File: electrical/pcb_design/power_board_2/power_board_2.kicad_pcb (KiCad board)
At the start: 4 copper layers, 82.5 x 82.5 mm, 92 parts, among them J1 STLINK, J2 Molex_504050-1291, J3 Molex_504050-1291, J4 Power Interconnect, Q1 CSD16342Q5A, Q2 CSD16342Q5A, Q3 CSD16342Q5A, U1 STM32L452RCTx, U2 TCAN330DR, U3 PAC1934T-I/JQ, U8 TPS63900

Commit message: finish initial component selection and start layout
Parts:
- removed BT1, BT2, BT3: Battery_Cell, footprints:BAT_1043
- removed JP13, JP2, JP4: SolderJumper_2_Open, Jumper:SolderJumper-2_P1.3mm_Open_RoundedPad1.0x1.5mm
- removed JP14: 0x10, Jumper:SolderJumper-2_P1.3mm_Open_RoundedPad1.0x1.5mm
- removed JP15: 0xEF, Jumper:SolderJumper-2_P1.3mm_Open_RoundedPad1.0x1.5mm
- removed Q1, Q2, Q3: CSD16342Q5A, Package_SON:VSON-8_3.3x3.3mm_P0.65mm_NexFET
- removed R10: 10m, Resistor_SMD:R_2512_6332Metric
- removed R13: 9k31, footprints:Nondescript_R_0402_1005Metric
- removed R51: 36k5, footprints:Nondescript_R_0603_1608Metric
- removed TH1: 10k NTC, footprints:Nondescript_R_0402_1005Metric
- removed TP7: TEMP, footprints:TestPoint_Pad_D1.5mm
- removed TP8: VBATT, footprints:TestPoint_Pad_D1.5mm
- added C18: 1u, footprints:Nondescript_C_0402_1005Metric, F.Cu at (159.8, 94.5)
- added C19: 4.7u, footprints:Nondescript_C_0402_1005Metric, F.Cu at (159.8, 96.5)
- added C20: 22n, footprints:Nondescript_C_0402_1005Metric, F.Cu at (173.3, 115.9)
- added C21: 22n, footprints:Nondescript_C_0402_1005Metric, F.Cu at (173.3, 117.9)
- added C22: 47u, footprints:Nondescript_C_0402_1005Metric, F.Cu at (173.3, 119.8)
- added C23: 1u, footprints:Nondescript_C_0402_1005Metric, F.Cu at (173.3, 121.8)
- added C24: 4.7u, footprints:Nondescript_C_0402_1005Metric, F.Cu at (173.3, 123.8)
- added C25: 10p, footprints:Nondescript_C_0402_1005Metric, F.Cu at (173.3, 125.7)
- added C26: 22n, footprints:Nondescript_C_0402_1005Metric, F.Cu at (173.3, 82.4)
- added C28: 47u, footprints:Nondescript_C_0402_1005Metric, F.Cu at (173.3, 86.4)
- added C29: 1u, footprints:Nondescript_C_0402_1005Metric, F.Cu at (173.3, 88.4)
- added C30: 4.7u, footprints:Nondescript_C_0402_1005Metric, F.Cu at (173.3, 90.3)
- added C31: 10p, footprints:Nondescript_C_0402_1005Metric, F.Cu at (173.3, 92.3)
- added C32: 22n, footprints:Nondescript_C_0402_1005Metric, F.Cu at (173.3, 99.2)
- added C33: 22n, footprints:Nondescript_C_0402_1005Metric, F.Cu at (173.3, 101.1)
- added C34: 47u, footprints:Nondescript_C_0402_1005Metric, F.Cu at (173.3, 103.1)
- added C35: 1u, footprints:Nondescript_C_0402_1005Metric, F.Cu at (173.3, 105.1)
- added C36: 4.7u, footprints:Nondescript_C_0402_1005Metric, F.Cu at (173.3, 107.0)
- added C37: 10p, footprints:Nondescript_C_0402_1005Metric, F.Cu at (173.3, 109.0)
- added D10: SM74611KTTR, footprints:SM74611, F.Cu at (101.6, 112.4)
- added D2: SM74611KTTR, footprints:SM74611, F.Cu at (65.3, 87.7)
- added D3: SM74611KTTR, footprints:SM74611, F.Cu at (65.3, 100.0)
- added D4: SM74611KTTR, footprints:SM74611, F.Cu at (65.3, 112.4)
- added D5: SM74611KTTR, footprints:SM74611, F.Cu at (83.4, 87.7)
- added D6: SM74611KTTR, footprints:SM74611, F.Cu at (83.4, 100.0)
- added D7: SM74611KTTR, footprints:SM74611, F.Cu at (83.4, 112.4)
- added D8: SM74611KTTR, footprints:SM74611, F.Cu at (101.6, 87.7)
- added D9: SM74611KTTR, footprints:SM74611, F.Cu at (101.6, 100.0)
- added J5: Molex_504050-0691, footprints:Molex_504050-0691, F.Cu at (68.6, 126.6)
- added J6: Molex_504050-0691, footprints:Molex_504050-0691, F.Cu at (68.6, 136.7)
- added JP7: SolderJumper_2_Open, Jumper:SolderJumper-2_P1.3mm_Open_RoundedPad1.0x1.5mm, F.Cu at (151.6, 112.8)
- added JP8: SolderJumper_2_Open, Jumper:SolderJumper-2_P1.3mm_Open_RoundedPad1.0x1.5mm, F.Cu at (151.6, 116.3)
- added JP9: SolderJumper_2_Open, Jumper:SolderJumper-2_P1.3mm_Open_RoundedPad1.0x1.5mm, F.Cu at (151.6, 119.9)
- added L2: 6.8u, footprints:LQH44PN_PR_MUR, F.Cu at (181.6, 124.6)
- added L3: 6.8u, footprints:LQH44PN_PR_MUR, F.Cu at (181.6, 91.1)
- added L4: 6.8u, footprints:LQH44PN_PR_MUR, F.Cu at (181.6, 107.9)
- added R11: 9k31, footprints:Nondescript_R_0402_1005Metric, F.Cu at (140.1, 111.8)
- added R12: 9k31, footprints:Nondescript_R_0402_1005Metric, F.Cu at (140.1, 113.8)
- added R15: 33, footprints:Nondescript_R_0402_1005Metric, F.Cu at (143.0, 105.9)
- added R16: 33, footprints:Nondescript_R_0402_1005Metric, F.Cu at (143.0, 107.8)
- added R18: 12k4, footprints:Nondescript_R_0402_1005Metric, F.Cu at (200.3, 99.0)
- added R19: 12k4, footprints:Nondescript_R_0402_1005Metric, F.Cu at (200.3, 101.0)
- added R42: 1M, footprints:Nondescript_R_0402_1005Metric, F.Cu at (176.2, 111.9)
- added R43: 1, Resistor_SMD:R_2512_6332Metric, F.Cu at (115.0, 93.7)
- added R44: 1, Resistor_SMD:R_2512_6332Metric, F.Cu at (115.0, 98.6)
- added R45: 1, Resistor_SMD:R_2512_6332Metric, F.Cu at (115.0, 103.5)
- added R46: 1, Resistor_SMD:R_2512_6332Metric, F.Cu at (115.0, 108.4)
- added U10: LTC3130EUDC-PBF, footprints:LTC3130, F.Cu at (186.3, 101.5)
- added U11: AD5242BRUZ1M, footprints:AD5242, F.Cu at (179.1, 101.6)
- added U12: PAC1932T-I/JQ, footprints:PAC1934, F.Cu at (77.1, 121.8)
- added U13: PAC1932T-I/JQ, footprints:PAC1934, F.Cu at (77.1, 128.0)
- added U4: BQ24075RGTR, footprints:BQ2407x, F.Cu at (163.9, 94.3)
- added U5: MCP4661-103E/ST, footprints:MCP4661, F.Cu at (153.8, 94.9)
- added U6: LTC3130EUDC-PBF, footprints:LTC3130, F.Cu at (186.3, 118.2)
- added U7: AD5242BRUZ1M, footprints:AD5242, F.Cu at (179.1, 118.3)
- added U9: AD5242BRUZ1M, footprints:AD5242, F.Cu at (179.1, 84.8)
- C1, C14, C6, C9: value 100n -> 1u; moved to F.Cu
- C10, C15, C16: value 1u -> 100n; moved to F.Cu
- C11: value 1u -> 22u; moved to F.Cu
- C12: value 1u -> 10u; moved to F.Cu
- C13: value 100n -> 22u; moved to F.Cu
- C17: value 100n -> 4.7u; moved to F.Cu
- C2, C3, C7, C8, D1, J2, J3, JP1, JP10, JP3, JP5, JP6, L1, R1, R3, R4, R6, R9, TP4, U1: moved to F.Cu
- C27: value 22u -> 22n; footprint footprints:Nondescript_C_0603_1608Metric -> footprints:Nondescript_C_0402_1005Metric; moved to F.Cu
- C4: value 10u -> 1u; footprint footprints:Nondescript_C_0603_1608Metric -> footprints:Nondescript_C_0402_1005Metric; moved to F.Cu
- C5: value 22u -> 100n; footprint footprints:Nondescript_C_0603_1608Metric -> footprints:Nondescript_C_0402_1005Metric; moved to F.Cu
- J4: value Power Interconnect -> Molex_504050-0691; moved to F.Cu
- PCB1: footprint footprints:Battery_Board_Shape_Space_Invader_2 -> footprints:Core_Board_Shape_Space_Invader_2
- R14, R25, R26: value 9k31 -> 33; moved to F.Cu
- R17: value 23k2 -> 33; moved to F.Cu
- R2, R5, R7, R8: value 33 -> 9k31; moved to F.Cu
- R20, R21: value 1k58 -> 1; footprint footprints:Nondescript_R_0402_1005Metric -> Resistor_SMD:R_2512_6332Metric; moved to F.Cu
- R22: value 23k2 -> 10m; footprint footprints:Nondescript_R_0402_1005Metric -> Resistor_SMD:R_2512_6332Metric; moved to F.Cu
- R23: value 9k31 -> 36k5; footprint footprints:Nondescript_R_0402_1005Metric -> footprints:Nondescript_R_0603_1608Metric; moved to F.Cu
- R24: value 10m -> 33; footprint Resistor_SMD:R_2512_6332Metric -> footprints:Nondescript_R_0402_1005Metric; moved to F.Cu
- R27: value 10m -> 60; footprint Resistor_SMD:R_2512_6332Metric -> footprints:Nondescript_R_0402_1005Metric; moved to F.Cu
- R28: value 9k31 -> 60; moved to F.Cu
- R29: value 10m -> 10k; footprint Resistor_SMD:R_2512_6332Metric -> footprints:Nondescript_R_0402_1005Metric; moved to F.Cu
- R30: value 9k31 -> 10m; footprint footprints:Nondescript_R_0402_1005Metric -> Resistor_SMD:R_2512_6332Metric; moved to F.Cu
- R31, R35: value 0 -> 4M; footprint Resistor_SMD:R_2512_6332Metric -> footprints:Nondescript_R_0402_1005Metric; moved to F.Cu
- R32, R36, R40: value 0 -> 200k; footprint Resistor_SMD:R_2512_6332Metric -> footprints:Nondescript_R_0402_1005Metric; moved to F.Cu
- R33, R41: value 0 -> 100k; footprint Resistor_SMD:R_2512_6332Metric -> footprints:Nondescript_R_0402_1005Metric; moved to F.Cu
- R34: value 0 -> 1M; footprint Resistor_SMD:R_2512_6332Metric -> footprints:Nondescript_R_0402_1005Metric; moved to F.Cu
- R37: value 33 -> 100k; moved to F.Cu
- R38: value 33 -> 1M; moved to F.Cu
- R39: value 33 -> 4M; moved to F.Cu
- R49, R50: value 60 -> 9k31; moved to F.Cu
- TP1: value VBUS -> BOARD_ID_POWER
- TP2: value BOARD_ID_POWER -> BOARD_ID_SENSE; moved to F.Cu
- TP3: value GND -> VBUS
- TP5: value BOARD_ID_SENSE -> +3V3; moved to F.Cu
- TP6: value +3V3 -> GND
- U2: value TCAN330DR -> TPS63900; footprint footprints:SOIC127P600X175-8N -> Package_SON:WSON-10-1EP_2.5x2.5mm_P0.5mm_EP1.2x2mm_ThermalVias; moved to F.Cu
- U3: value PAC1934T-I/JQ -> TCAN330DR; footprint footprints:UQFN-16-1EP_4x4mm_P0.65mm_EP2.6x2.6mm -> footprints:SOIC127P600X175-8N; moved to F.Cu
- U8: value TPS63900 -> LTC3130EUDC-PBF; footprint Package_SON:WSON-10-1EP_2.5x2.5mm_P0.5mm_EP1.2x2mm -> footprints:LTC3130; moved to F.Cu
- moved PCB1 103.9 mm to (33.9, 80.8)
- moved R49 81.9 mm to (75.4, 132.1), turned to 0 degrees
- moved R50 79.6 mm to (75.4, 134.1), turned to 0 degrees
- moved J1 79.2 mm to (197.9, 109.6), turned to 0 degrees
- moved TP6 76.4 mm to (192.7, 93.9)
- moved R24 70.6 mm to (192.4, 108.1), turned to 0 degrees
- moved R37 61.6 mm to (176.2, 93.2), turned to 0 degrees
- moved TP2 57.1 mm to (192.7, 103.3), turned to 0 degrees
- moved R22 55.7 mm to (198.9, 89.8), turned to 0 degrees
- moved J2 55.3 mm to (134.4, 86.1), turned to 0 degrees
- moved R39 55.1 mm to (176.2, 105.9), turned to 0 degrees
- moved TP5 54.9 mm to (192.7, 90.3), turned to 0 degrees
- moved R38 54.6 mm to (176.2, 95.2), turned to 0 degrees
- moved U2 54.5 mm to (200.2, 83.8), turned to 0 degrees
- moved R35 53.5 mm to (176.2, 89.2)
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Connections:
- C1 pad 1: /NRST -> +3V3
- C10 pad 1: +3V3 -> /BOOT0
- C11 pad 1: +3V3 -> VBUS
- C12 pad 1: +3V3 -> VBUS
- C13 pad 1: +3V3 -> /Charger/BOARD_load+
- C16 pad 1: +3V3 -> GND
- C16 pad 2: GND -> Net-(C16-Pad2)
- C17 pad 1: +3V3 -> Net-(C17-Pad1)
- C2 pad 1: /BOOT0 -> +3V3
- C27 pad 1: VBUS -> Net-(U8-BST2)
- C27 pad 2: GND -> Net-(U8-SW2)
- C3 pad 1: GND -> +3V3
- C3 pad 2: Net-(C3-Pad2) -> GND
- C4 pad 1: VBUS -> +3V3
- C5 pad 1: /Batteries/BOARD_LOAD_+ -> /NRST
- J4 pad 1: GND -> Net-(C17-Pad1)
- J4 pad 2: GND -> Net-(C17-Pad1)
- J4 pad 3: GND -> Net-(C17-Pad1)
- J4 pad 4: VBATT -> GND
- J4 pad 5: VBATT -> GND
- J4 pad 6: VBATT -> GND
- JP1 pad 1: /CANH_UPSTREAM -> Net-(JP1-A)
- JP1 pad 2: Net-(JP1-B) -> /Board Identification/BOARD_ID_POWER
- JP10 pad 1: /Board Identification/BOARD_ID_SENSE -> /CAN bus/CANL_TERMINATION
- JP3 pad 1: Net-(JP1-B) -> /Board Identification/BOARD_ID_SENSE
- JP3 pad 2: /CAN bus/CANH_TERMINATION -> Net-(JP3-B)
- JP5 pad 1: Net-(JP1-B) -> Net-(JP5-A)
- JP5 pad 2: /CANH_DOWNSTREAM -> /CAN bus/CANH_TERMINATION
- JP6 pad 1: Net-(JP2-B) -> /CANH_UPSTREAM
- JP6 pad 2: /CANL_DOWNSTREAM -> Net-(JP5-A)
- L1 pad 1: Net-(U8-LX2) -> Net-(U2-LX2)
- L1 pad 2: Net-(U8-LX1) -> Net-(U2-LX1)
- R14 pad 1: +3V3 -> Net-(U1-PB13)
- R14 pad 2: /Batteries/I2C_SCL -> /CTRL.SWCLK
- R17 pad 1: Net-(JP14-B) -> Net-(U1-PB15)
- R17 pad 2: Net-(JP10-B) -> /CTRL.SWDIO
- R2 pad 1: Net-(D1-K) -> /BOOT0
- R20 pad 1: Net-(JP10-B) -> /Charger/Solar and Sense/SSx2
- R20 pad 2: GND -> /Charger/Solar and Sense/Solar_x2+
- R21 pad 1: Net-(JP15-B) -> /Charger/Solar and Sense/Solar_x1+
- R21 pad 2: Net-(JP13-B) -> /Charger/Solar and Sense/SSx1
- R22 pad 1: Net-(JP13-B) -> /Charger/BOARD_load+
- R22 pad 2: GND -> +3V3
- R23 pad 1: VBATT -> Net-(U2-CFG1)
- R23 pad 2: /Batteries/BATTERY_1_EN -> GND
- R24 pad 1: VBATT -> /SWDIO
- R24 pad 2: /Batteries/B1+ -> Net-(J1-T_SWDIO)
- R25 pad 1: +3V3 -> /NRST
- R25 pad 2: Net-(U3-SLOW) -> Net-(J1-T_NRST)
- R26 pad 1: VBATT -> /SWCLK
- R26 pad 2: /Batteries/BATTERY_2_EN -> Net-(J1-T_SWCLK)
- R27 pad 1: VBATT -> /CAN bus/CANH_TERMINATION
- R27 pad 2: /Batteries/B2+ -> Net-(C16-Pad2)
- R28 pad 1: VBATT -> Net-(C16-Pad2)
- R28 pad 2: /Batteries/BATTERY_3_EN -> /CAN bus/CANL_TERMINATION
- R29 pad 1: VBATT -> Net-(U4-TS)
- R29 pad 2: /Batteries/B3+ -> GND
- R3 pad 1: /BOOT0 -> +3V3
- R3 pad 2: GND -> /SWDIO
- R30 pad 1: +3V3 -> VBUS
- R30 pad 2: /Batteries/TEMPERATURE_SENSE -> /Charger/BUS_Load+
- R31 pad 1: Net-(BT1-PadN) -> /Charger/Solar and Sense/MPPT_1/VOUT
- R31 pad 2: Net-(Q1-D) -> /Charger/Solar and Sense/MPPT_1/CHRG_CTRL_1
- R32 pad 1: Net-(BT1-PadN) -> Net-(C25-Pad2)
- R32 pad 2: GND -> /Charger/Solar and Sense/MPPT_1/CHRG_CTRL_1
- R33 pad 1: Net-(BT2-PadN) -> /Charger/Solar and Sense/MPPT_1/MPPT_1_DP_W
- R33 pad 2: Net-(Q2-D) -> GND
- R34 pad 1: Net-(BT2-PadN) -> /Charger/Solar and Sense/MPPT_1/CHRG_CTRL_1
- R35 pad 1: Net-(BT3-PadN) -> /Charger/Solar and Sense/MPPT_2/VOUT
- R35 pad 2: Net-(Q3-D) -> /Charger/Solar and Sense/MPPT_2/CHRG_CTRL_2
- R36 pad 1: Net-(BT3-PadN) -> Net-(C31-Pad2)
- R36 pad 2: GND -> /Charger/Solar and Sense/MPPT_2/CHRG_CTRL_2
- R37 pad 1: /NRST -> /Charger/Solar and Sense/MPPT_2/MPPT_2_DP_W
- R37 pad 2: Net-(J1-T_NRST) -> GND
- R38 pad 1: /SWDIO -> /Charger/Solar and Sense/MPPT_2/CHRG_CTRL_2
- R38 pad 2: Net-(J1-T_SWDIO) -> GND
- R39 pad 1: /SWCLK -> /Charger/Solar and Sense/MPPT_3/VOUT
- R39 pad 2: Net-(J1-T_SWCLK) -> /Charger/Solar and Sense/MPPT_3/CHRG_CTRL_3
- R40 pad 1: VBUS -> Net-(C37-Pad2)
- R40 pad 2: VBATT -> /Charger/Solar and Sense/MPPT_3/CHRG_CTRL_3
- R41 pad 1: VBUS -> /Charger/Solar and Sense/MPPT_3/MPPT_3_DP_W
- R41 pad 2: VBATT -> GND
- R49 pad 1: /CAN bus/CANH_TERMINATION -> +3V3
- R49 pad 2: Net-(C3-Pad2) -> Net-(U12-SLOW/*ALERT)
- R5 pad 1: Net-(U1-PB14) -> +3V3
- R5 pad 2: /CTRL.NRST -> /Charger/I2C3_SLC
- R50 pad 1: Net-(C3-Pad2) -> +3V3
- R50 pad 2: /CAN bus/CANL_TERMINATION -> Net-(U13-SLOW/*ALERT)
- R6 pad 2: /SWDIO -> /Charger/I2C3_SDA
- R7 pad 1: Net-(U1-PB9) -> +3V3
- R7 pad 2: /CTRL.BOOT0 -> /Charger/I2C1_SLC
- R8 pad 1: Net-(U1-PB13) -> +3V3
- R8 pad 2: /CTRL.SWCLK -> /Charger/I2C1_SDA
- R9 pad 1: Net-(U1-PB15) -> Net-(U1-PB9)
- R9 pad 2: /CTRL.SWDIO -> /CTRL.BOOT0
- TP1 pad 1: VBUS -> /Board Identification/BOARD_ID_POWER
- TP2 pad 1: /Board Identification/BOARD_ID_POWER -> /Board Identification/BOARD_ID_SENSE
- TP3 pad 1: GND -> VBUS
- TP4 pad 1: /Batteries/BOARD_LOAD_+ -> /Charger/BOARD_load+
- TP5 pad 1: /Board Identification/BOARD_ID_SENSE -> +3V3
- TP6 pad 1: +3V3 -> GND
- U1 pad 21: /Batteries/TEMPERATURE_SENSE -> unconnected-(U1-PA5-Pad21)
- U1 pad 26: unconnected-(U1-PB0-Pad26) -> /Charger/CHRG_STATUS
- U1 pad 27: unconnected-(U1-PB1-Pad27) -> /Charger/BATT_CHRG_EN
- U1 pad 28: unconnected-(U1-PB2-Pad28) -> /Charger/PWR_STATUS
- U1 pad 29: /Batteries/I2C_SCL -> /Charger/I2C2_SLC
- U1 pad 30: /Batteries/I2C_SDA -> /Charger/I2C2_SDA
- U1 pad 50: unconnected-(U1-PA15-Pad50) -> /Charger/WP
- U1 pad 56: /Batteries/BATTERY_3_EN -> /Charger/MPPT_3_STATUS
- U1 pad 57: /Batteries/BATTERY_2_EN -> /Charger/MPPT_2_STATUS
- U1 pad 58: /MCU/I2C1_SCL -> /Charger/I2C1_SLC
- U1 pad 59: /MCU/I2C1_SDA -> /Charger/I2C1_SDA
- U1 pad 61: /Batteries/BATTERY_1_EN -> /Charger/MPPT_1_STATUS
- U1 pad 8: /MCU/I2C3_SCL -> /Charger/I2C3_SLC
- U1 pad 9: /MCU/I2C3_SDA -> /Charger/I2C3_SDA
- U2 pad 1: /CAN bus/CAN_TX -> VBUS
- U2 pad 2: GND -> VBUS
- U2 pad 3: +3V3 -> Net-(U2-CFG1)
- U2 pad 4: /CAN bus/CAN_RX -> GND
- U2 pad 5: /CAN bus/CAN_SHUTDOWN -> GND
- U2 pad 6: Net-(JP2-B) -> /Charger/BOARD_load+
- U2 pad 7: Net-(JP1-B) -> Net-(U2-LX2)
- U2 pad 8: /CAN bus/CAN_SILENT -> GND
- U3 pad 1: Net-(U3-SLOW) -> /CAN bus/CAN_TX
- U3 pad 2: +3V3 -> GND
- U3 pad 3: GND -> +3V3
- U3 pad 4: /Batteries/I2C_SCL -> /CAN bus/CAN_RX
- U3 pad 5: /Batteries/I2C_SDA -> /CAN bus/CAN_SHUTDOWN
- U3 pad 6: GND -> Net-(JP10-B)
- U3 pad 7: VBATT -> Net-(JP5-A)
- U3 pad 8: /Batteries/B1+ -> /CAN bus/CAN_SILENT
- U8 pad 1: VBUS -> Net-(U8-BST1)
- U8 pad 10: VBUS -> Net-(U8-VCC)
- U8 pad 2: VBUS -> /Charger/Solar and Sense/SSy1
- U8 pad 3: Net-(U8-CFG1) -> /Charger/Solar and Sense/SSy1
- U8 pad 4: GND -> /Charger/Solar and Sense/SSy1
- U8 pad 5: GND -> Net-(U8-VCC)
- U8 pad 6: /Batteries/BOARD_LOAD_+ -> /Charger/Solar and Sense/MPPT_2/MPPT_2_DP_W
- U8 pad 7: Net-(U8-LX2) -> GND
- U8 pad 9: Net-(U8-LX1) -> /Charger/Solar and Sense/MPPT_2/CHRG_CTRL_2
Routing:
- net /SWDIO: track 92.6 -> 0.00 mm, vias 3 -> 0
- net /SWCLK: track 88.7 -> 0.00 mm, vias 2 -> 0
- net /NRST: track 87.7 -> 0.00 mm, vias 2 -> 0
- net /Batteries/BATTERY_3_EN: track 76.0 -> 0.00 mm, vias 3 -> 0
- net /SWO: track 74.8 -> 0.00 mm, vias 3 -> 0
- net GND: track 67.6 -> 0.00 mm, vias 152 -> 0
- net /Batteries/BATTERY_2_EN: track 66.1 -> 0.00 mm, vias 3 -> 0
- net /Batteries/BATTERY_1_EN: track 64.8 -> 0.00 mm, vias 4 -> 0
- net /CTRL.SWO: track 55.3 -> 0.00 mm, vias 4 -> 0
- net /CTRL.SWCLK: track 53.8 -> 0.00 mm, vias 2 -> 0
- net /CTRL.NRST: track 53.4 -> 0.00 mm, vias 2 -> 0
- net /CTRL.SWDIO: track 53.2 -> 0.00 mm, vias 2 -> 0
- net +3V3: track 48.0 -> 0.00 mm, vias 33 -> 0
- net VBATT: track 44.5 -> 0.00 mm, vias 1 -> 0
- net /MCU/DEBUG_LED: track 42.6 -> 0.00 mm, vias 2 -> 0
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- removed copper zone on B.Cu, net +3V3
- removed copper zone on In2.Cu, net +3V3
- removed copper zone on B.Cu, net /Batteries/B1+
- removed copper zone on B.Cu, net /Batteries/B2+
- removed copper zone on B.Cu, net /Batteries/B3+
- removed copper zone on B.Cu, net /Batteries/BOARD_LOAD_+
- removed copper zone on B.Cu, net GND
- removed copper zone on F.Cu, net GND
- removed copper zone on In1.Cu, net GND
- removed copper zone on B.Cu, net Net-(BT1-PadN)
- removed copper zone on B.Cu, net Net-(BT2-PadN)
- removed copper zone on B.Cu, net Net-(BT3-PadN)
- removed copper zone on B.Cu, net Net-(Q1-D)
- removed copper zone on B.Cu, net Net-(Q2-D)
- removed copper zone on B.Cu, net Net-(Q3-D)
- removed copper zone on B.Cu, net VBATT
- removed copper zone on B.Cu, net VBUS
- removed copper zone on F.Cu, net VBUS
- removed copper zone on In2.Cu, net VBUS
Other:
- outline, holes or cut-outs redrawn
- board text removed: "Board ID"
- board text removed: "CAN Termination"
- board text removed: "Downstream CAN"
- board text removed: "Upstream CAN"

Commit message: start layout
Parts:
- J3: moved to B.Cu
- moved PCB1 124.7 mm to (126.3, 164.7)
- moved J2 83.8 mm to (194.5, 144.3), turned to 90 degrees
- moved C1 75.6 mm to (188.2, 62.1)
- moved C10 75.6 mm to (191.1, 69.9)
- moved C11 75.6 mm to (247.0, 26.7)
- moved C12 75.6 mm to (247.0, 28.7)
- moved C13 75.6 mm to (247.0, 30.7)
- moved C14 75.6 mm to (206.2, 55.7)
- moved C15 75.6 mm to (206.2, 57.7)
- moved C16 75.6 mm to (206.2, 59.7)
- moved C2 75.6 mm to (188.2, 64.0)
- moved C20 75.6 mm to (224.3, 60.2)
- moved C22 75.6 mm to (224.3, 64.1)
- moved C23 75.6 mm to (224.3, 66.1)
- moved C26 75.6 mm to (224.3, 26.7)
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
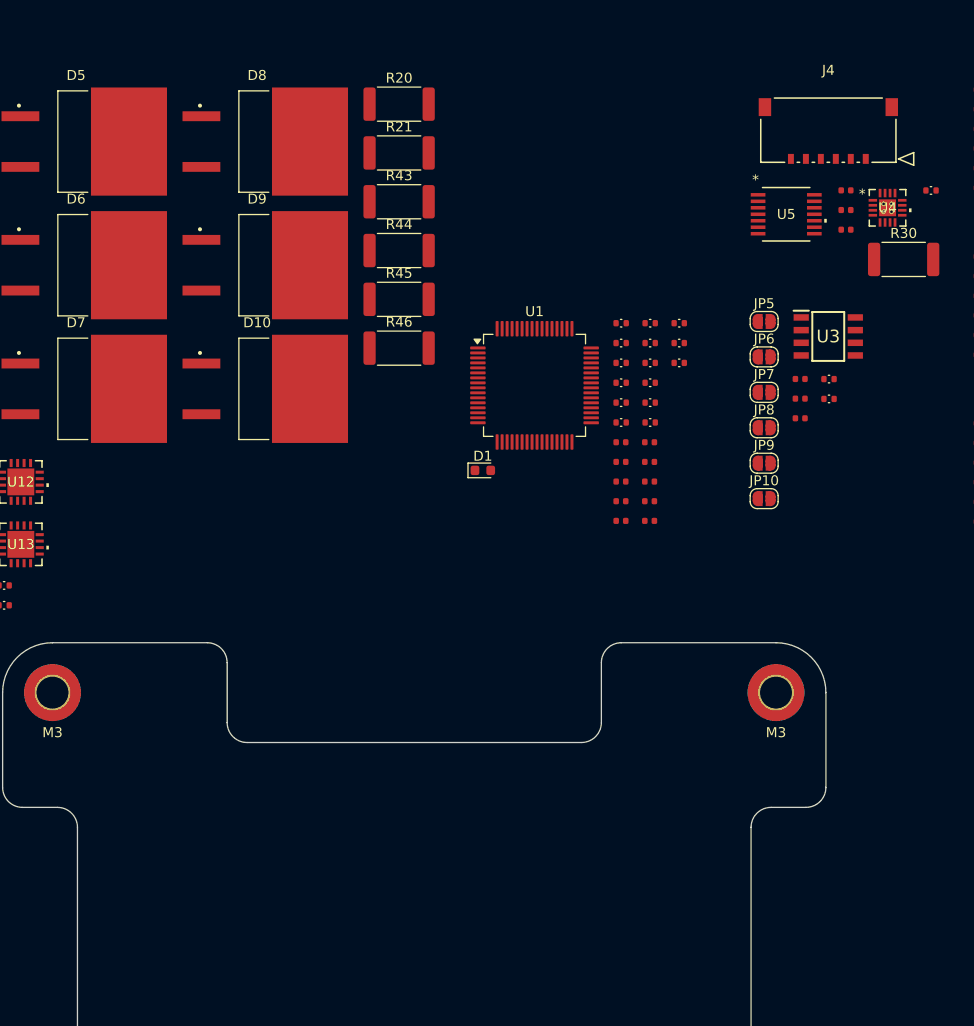
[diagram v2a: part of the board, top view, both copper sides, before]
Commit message: battery port placement
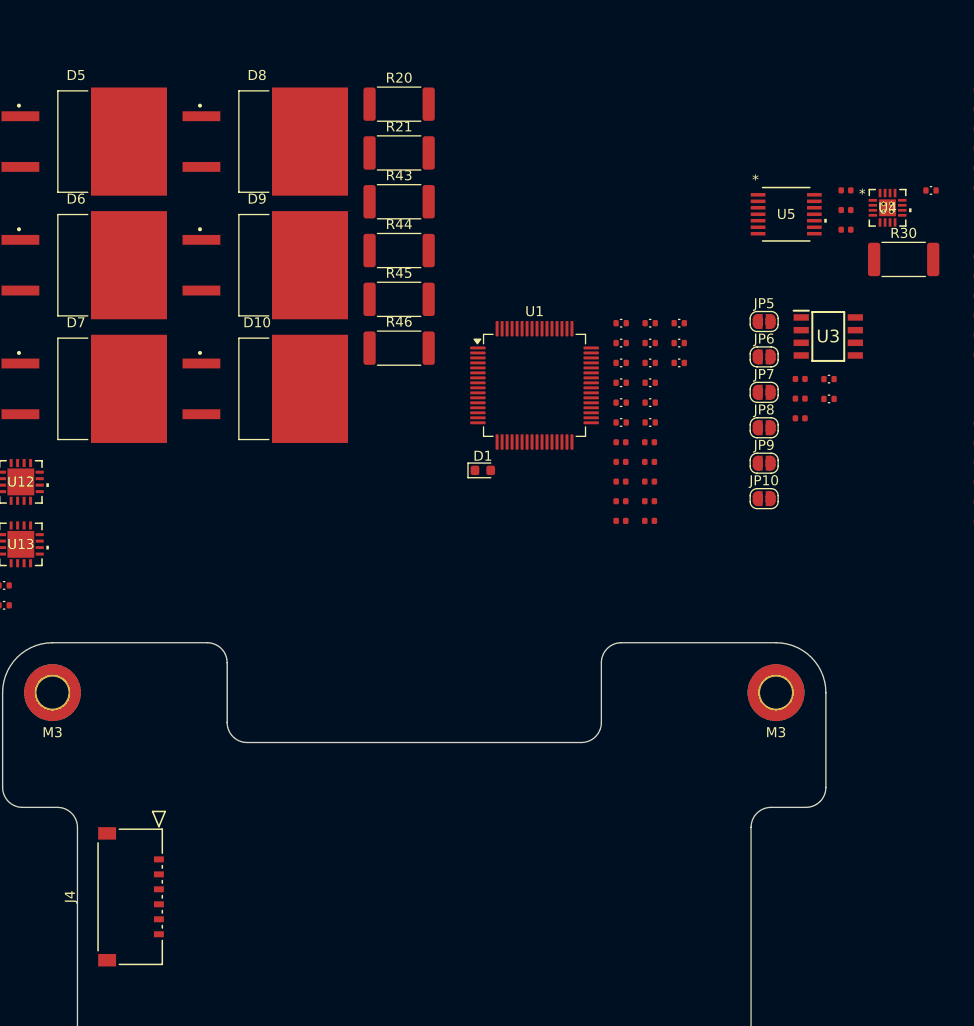
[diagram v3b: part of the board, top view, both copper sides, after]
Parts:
- moved J4 99.7 mm to (141.9, 103.9), turned to 90 degrees

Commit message: halfway through component layout part 1
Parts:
- C32, C33, C34, C35, C36, C37, D10, D4, D7, D8, D9, J6, L4, R39, R40, R41, R42, R45, R46, U10, U11: moved to B.Cu
- moved U8 131.0 mm to (171.6, 142.3), turned to -90 degrees
- moved U9 128.7 mm to (165.7, 140.5), turned to -90 degrees
- moved C27 127.2 mm to (173.0, 145.0), turned to 180 degrees
- moved R35 126.4 mm to (169.8, 146.1), turned to 180 degrees
- moved R36 125.0 mm to (168.2, 145.6), turned to -90 degrees
- moved C26 123.8 mm to (173.6, 139.6)
- moved R38 122.0 mm to (167.1, 145.6), turned to 90 degrees
- moved C31 121.4 mm to (169.8, 145.0), turned to 180 degrees
- moved C28 120.9 mm to (170.0, 138.6), turned to 180 degrees
- moved L3 120.8 mm to (176.8, 142.6), turned to -90 degrees
- moved C30 118.2 mm to (170.0, 139.6), turned to 180 degrees
- moved C29 117.5 mm to (173.6, 138.6)
- moved R37 116.0 mm to (166.0, 136.1), turned to 180 degrees
- moved U6 114.5 mm to (154.5, 141.6), turned to -90 degrees
- moved U7 112.6 mm to (148.2, 139.8), turned to -90 degrees
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
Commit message: initial power component layout
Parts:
- C17, C18, C19, R29, R30, U4, U5: moved to B.Cu
- moved C11 148.1 mm to (206.5, 169.2)
- moved C12 148.1 mm to (206.5, 171.2)
- moved C13 148.1 mm to (206.5, 173.2)
- moved J1 148.1 mm to (208.5, 196.4)
- moved JP1 148.1 mm to (207.3, 186.6)
- moved JP3 148.1 mm to (207.3, 190.1)
- moved L1 148.1 mm to (207.6, 180.9)
- moved R18 148.1 mm to (210.9, 185.8)
- moved R22 148.1 mm to (209.4, 176.6)
- moved R23 148.1 mm to (212.1, 180.3)
- moved R24 148.1 mm to (203.0, 194.9)
- moved R25 148.1 mm to (203.0, 196.9)
- moved R26 148.1 mm to (203.0, 198.8)
- moved TP1 148.1 mm to (203.3, 186.6)
- moved TP2 148.1 mm to (203.3, 190.1)
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
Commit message: mcu placement
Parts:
- removed TP3: VBUS, footprints:TestPoint_Pad_D1.5mm
- removed TP4: BOARD_LOAD_+, footprints:TestPoint_Pad_D1.5mm
- removed TP5: +3V3, footprints:TestPoint_Pad_D1.5mm
- removed TP6: GND, footprints:TestPoint_Pad_D1.5mm
- added J7: Molex_504050-0691, footprints:Molex_504050-0691, B.Cu at (141.9, 111.5)
- C1, C10, C2, C3, C4, C5, C6, C7, C8, C9, D1, JP1, JP3, R1, R11, R12, R14, R15, R16, R17, R18, R19, R2, R3, R4, R5, R6, R7, R8, R9, TP1, TP2, U1: moved to B.Cu
- moved R15 138.0 mm to (211.8, 146.4), turned to 180 degrees
- moved D1 136.6 mm to (211.1, 144.8), turned to 180 degrees
- moved C8 112.0 mm to (187.9, 158.1)
- moved R1 111.0 mm to (187.4, 153.9), turned to 180 degrees
- moved R5 111.0 mm to (187.4, 154.9), turned to 180 degrees
- moved R6 111.0 mm to (187.4, 155.9), turned to 180 degrees
- moved C5 110.9 mm to (187.4, 152.9), turned to 0 degrees
- moved C9 110.0 mm to (186.9, 158.1)
- moved C3 107.0 mm to (185.3, 148.8)
- moved R9 106.6 mm to (184.8, 147.1), turned to 0 degrees
- moved C4 105.1 mm to (184.3, 148.8)
- moved C10 104.5 mm to (184.9, 146.0), turned to 0 degrees
- moved R2 103.3 mm to (184.8, 145.0), turned to 0 degrees
- moved R8 99.7 mm to (182.4, 144.1)
- moved R7 97.7 mm to (181.4, 144.1)
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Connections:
- D2 pad 1: /Charger/Solar and Sense/Solar_x2- -> GND
- D2 pad 3: /Charger/Solar and Sense/Solar_x2- -> GND
- D5 pad 1: /Charger/Solar and Sense/Solar_y2- -> GND
- D5 pad 3: /Charger/Solar and Sense/Solar_y2- -> GND
- D8 pad 1: /Charger/Solar and Sense/Solar_z2- -> GND
- D8 pad 3: /Charger/Solar and Sense/Solar_z2- -> GND
- J6 pad 2: /Charger/Solar and Sense/Solar_x2- -> GND
- J6 pad 4: /Charger/Solar and Sense/Solar_y2- -> GND
- J6 pad 6: /Charger/Solar and Sense/Solar_z2- -> GND
- U1 pad 26: /Charger/CHRG_STATUS -> unconnected-(U1-PB0-Pad26)
- U1 pad 27: /Charger/BATT_CHRG_EN -> unconnected-(U1-PB1-Pad27)
- U1 pad 28: /Charger/PWR_STATUS -> unconnected-(U1-PB2-Pad28)
- U1 pad 40: unconnected-(U1-PC9-Pad40) -> /Charger/MPPT_1_STATUS
- U1 pad 41: unconnected-(U1-PA8-Pad41) -> /Charger/MPPT_2_STATUS
- U1 pad 54: unconnected-(U1-PD2-Pad54) -> /Charger/CHRG_STATUS
- U1 pad 56: /Charger/MPPT_3_STATUS -> /Charger/BATT_CHRG_EN
- U1 pad 57: /Charger/MPPT_2_STATUS -> /Charger/PWR_STATUS
- U1 pad 61: /Charger/MPPT_1_STATUS -> /Charger/MPPT_3_STATUS

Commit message: component layout
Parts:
- C11, C12, C13, C14, C15, C16, JP10, JP5, JP7, JP9, L1, R22, R23, R27, R28, U2, U3: moved to B.Cu
- moved R50 117.1 mm to (193.8, 84.4)
- moved U13 107.6 mm to (192.7, 87.6), turned to -90 degrees
- moved R49 104.6 mm to (142.8, 84.3)
- moved U12 97.5 mm to (141.8, 87.5), turned to -90 degrees
- moved R23 86.9 mm to (168.1, 105.3), turned to 90 degrees
- moved L1 80.9 mm to (174.3, 107.2), turned to -90 degrees
- moved C13 77.2 mm to (170.8, 104.6), turned to 180 degrees
- moved C12 77.0 mm to (165.8, 105.9), turned to 90 degrees
- moved U2 75.3 mm to (170.9, 106.7)
- moved C11 74.8 mm to (166.8, 105.9), turned to 90 degrees
- moved R22 72.1 mm to (180.1, 110.8), turned to -90 degrees
- moved JP9 45.8 mm to (158.7, 150.7), turned to 180 degrees
- moved JP8 45.0 mm to (184.2, 140.3), turned to 180 degrees
- moved C15 44.9 mm to (163.6, 144.4), turned to 180 degrees
- moved C14 42.5 mm to (163.6, 145.4), turned to 180 degrees
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
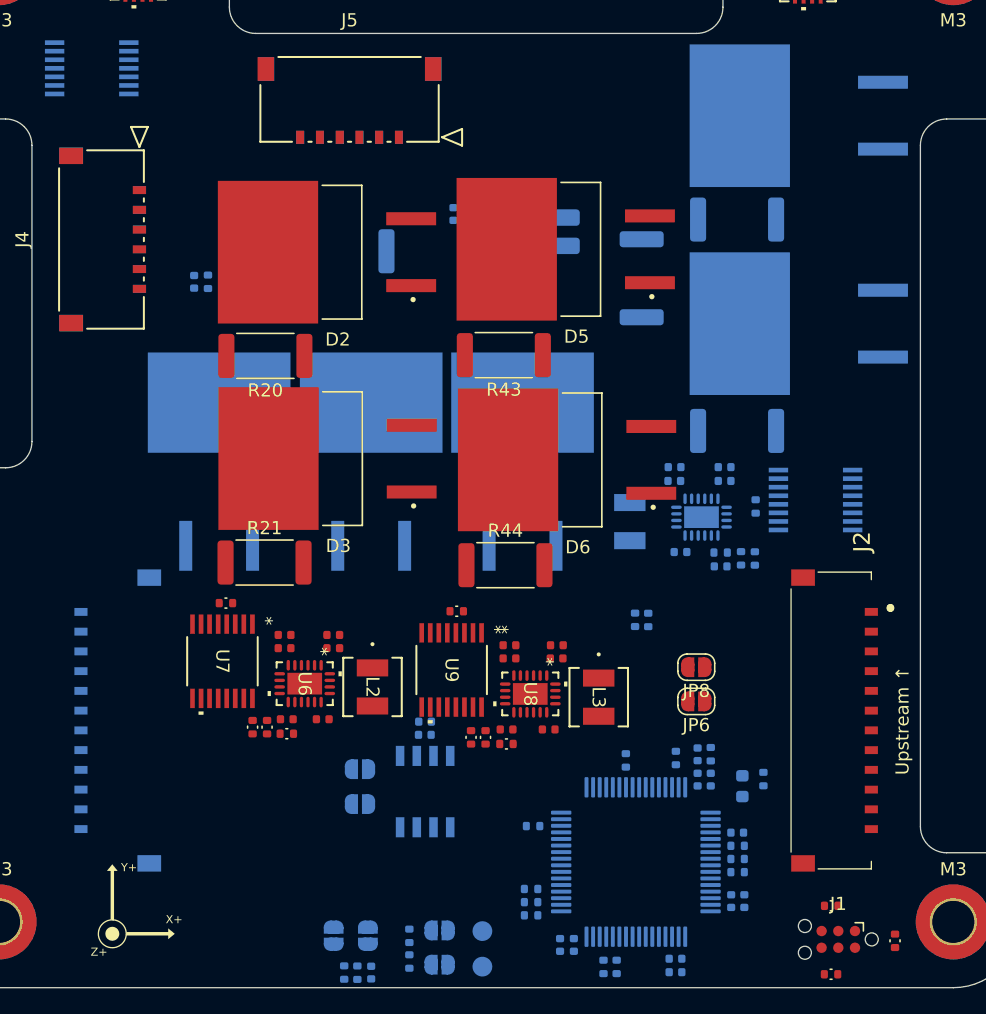
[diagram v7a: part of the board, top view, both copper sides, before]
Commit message: mppt traces
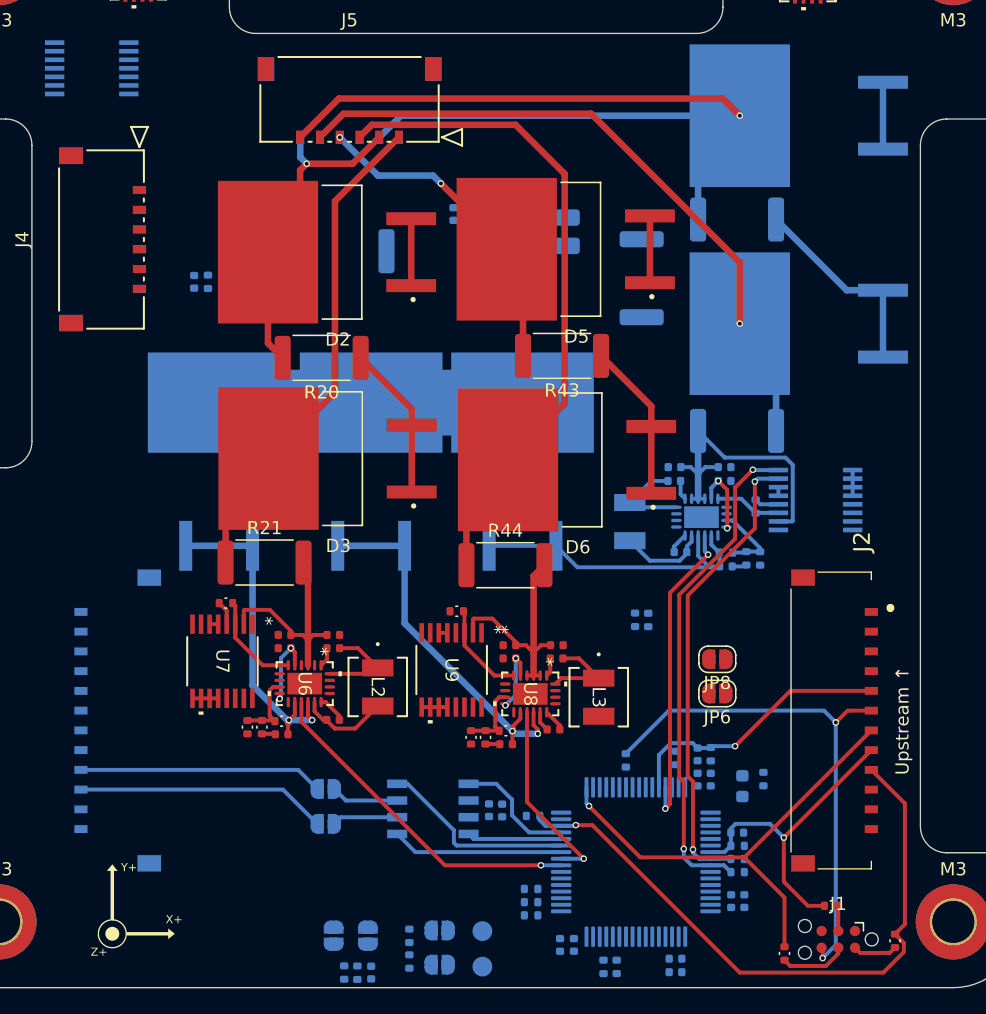
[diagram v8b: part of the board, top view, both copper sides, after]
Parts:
- moved C15 8.93 mm to (169.5, 151.2), turned to 90 degrees
- moved C14 7.52 mm to (168.5, 151.2), turned to 90 degrees
- moved R43 4.42 mm to (174.0, 116.7)
- moved R20 4.28 mm to (155.8, 116.8)
- moved R26 3.88 mm to (190.9, 162.1), turned to -90 degrees
- moved JP7 3.00 mm to (156.1, 149.6)
- moved JP9 3.00 mm to (156.1, 152.2)
- moved JP8 1.71 mm to (185.8, 139.7)
- moved JP6 1.71 mm to (185.8, 142.3)
- moved U3 1.44 mm to (164.2, 151.1), turned to 180 degrees
- moved C25 1.21 mm to (152.7, 145.4)
- moved C31 1.12 mm to (169.8, 146.2)
- moved R31 1.03 mm to (152.7, 144.4)
- moved R35 1.00 mm to (169.8, 145.1)
- moved C21 0.78 mm to (156.6, 144.3)
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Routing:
- net /Charger/Solar and Sense/Solar_z2+: track 0.00 -> 72.4 mm, vias 0 -> 1
- net /Charger/Solar and Sense/Solar_z1+: track 0.00 -> 51.3 mm, vias 0 -> 1
- net /Charger/Solar and Sense/Solar_y1+: track 0.00 -> 50.4 mm
- net /SWDIO: track 0.00 -> 48.9 mm, vias 0 -> 1
- net /SWO: track 0.00 -> 39.9 mm, vias 0 -> 2
- net /Charger/I2C3_SDA: track 0.00 -> 37.9 mm, vias 0 -> 2
- net /Charger/Solar and Sense/Solar_x1+: track 0.00 -> 37.8 mm
- net /SWCLK: track 0.00 -> 36.6 mm, vias 0 -> 1
- net /Charger/I2C3_SLC: track 0.00 -> 35.4 mm, vias 0 -> 2
- net /Charger/Solar and Sense/MPPT_2/VOUT: track 0.00 -> 29.0 mm, vias 0 -> 2
- net /Charger/MPPT_1_STATUS: track 0.00 -> 25.8 mm, vias 0 -> 1
- net /Charger/Solar and Sense/MPPT_1/VOUT: track 0.00 -> 25.5 mm, vias 0 -> 2
- net /Charger/Solar and Sense/Solar_x2+: track 0.00 -> 25.0 mm, vias 0 -> 1
- net /Charger/Solar and Sense/Solar_y2+: track 0.00 -> 24.8 mm, vias 0 -> 2
- net GND: track 0.00 -> 24.8 mm
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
